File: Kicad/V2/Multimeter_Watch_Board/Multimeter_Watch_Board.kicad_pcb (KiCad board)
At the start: 4 copper layers, 46 x 42 mm, 52 parts, among them J1 S3B-PH-K-S(LF)(SN), J2 S3B-PH-K-S(LF)(SN), J3 S3B-PH-K-S(LF)(SN), J6 51281-1294, J7 Conn_01x11_Female, J8 Conn_01x11_Female, Q1 A03400A N-MOS, U1 PCF85163-SO08, U2 AD8592, Y1 32kHz

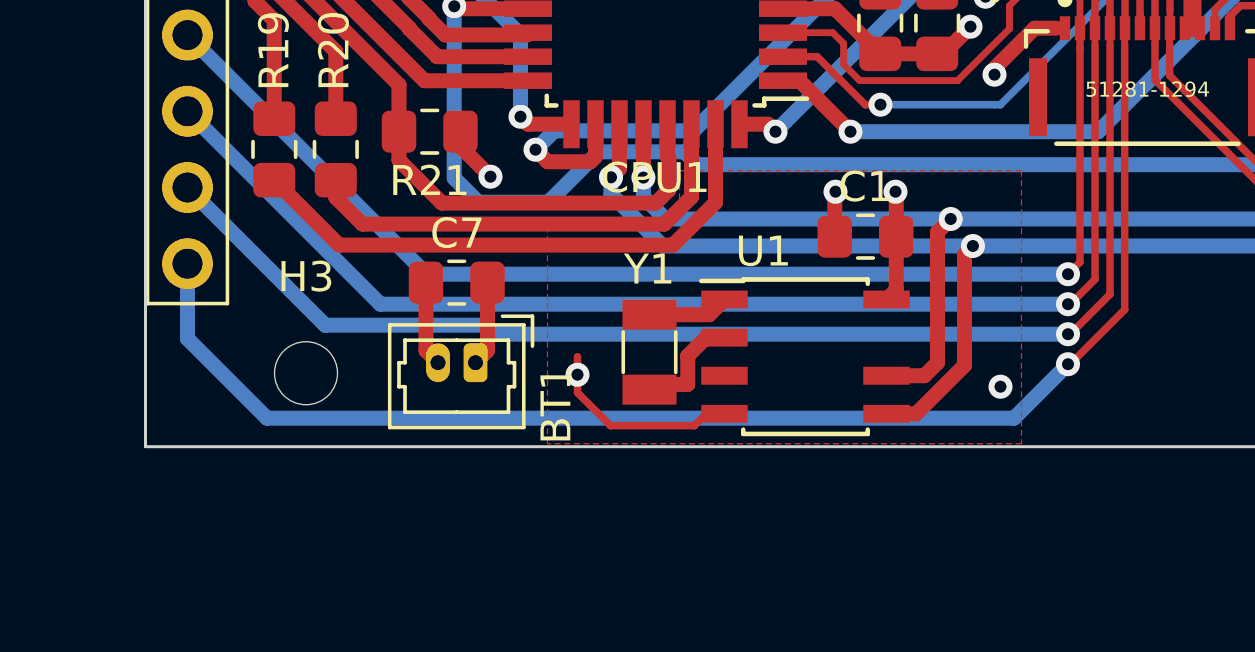
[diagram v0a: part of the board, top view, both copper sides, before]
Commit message: move battery connector, fix silkscreen labeling of females
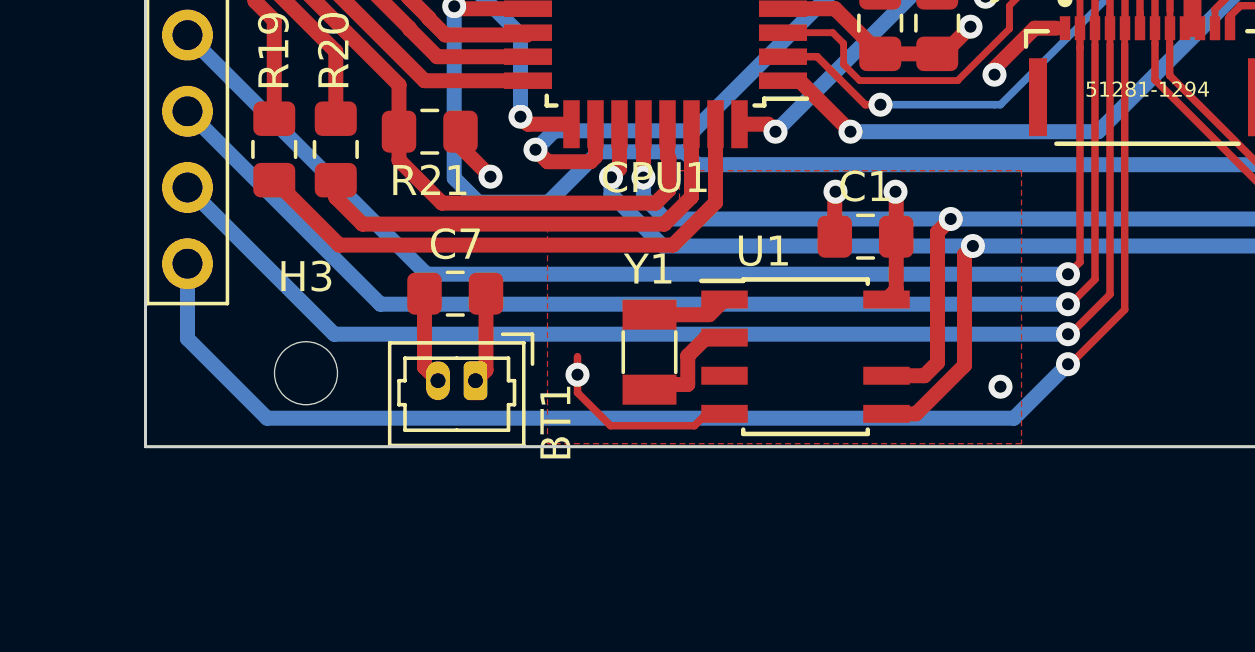
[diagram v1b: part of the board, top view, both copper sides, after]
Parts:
- moved BT1 0.60 mm to (113.0, 97.8)
- moved C7 0.37 mm to (112.3, 94.9)
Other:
- board text added: "PB6"
- board text added: "PB7"
- board text added: "PD5"
- board text added: "PD6"
- board text added: "PE5"

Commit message: Swiss cheese optimalizations
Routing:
- net /GND: track 38.9 -> 45.7 mm
- net /PB6: track 55.7 -> 59.6 mm
- net /PB7: track 59.6 -> 62.9 mm
- net /PE5: track 53.7 -> 57.0 mm
- net /ADC3: track 61.2 -> 63.0 mm
- net /ADC6: track 62.0 -> 60.2 mm
- net /PE4: track 54.9 -> 56.4 mm
- net /PD3: track 47.5 -> 48.8 mm
- net /VCC: track 32.7 -> 33.1 mm, vias 6 -> 5
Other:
- board text added: "PE4"

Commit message: change voltage/current connector setup from pins 1-2 to 1-3 for greater distance between voltage input pins
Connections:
- J3 pad 2: /ADC1 -> Net-(J3-Pad2)
- J3 pad 3: Net-(J3-Pad3) -> /ADC1
- R1 pad 1: Net-(J2-Pad2) -> Net-(J2-Pad3)
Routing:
- net Net-(J2-Pad2): track 6.22 -> 0.00 mm
- net Net-(J2-Pad3): track 0.00 -> 4.77 mm
- net /ADC1: track 40.3 -> 38.1 mm
